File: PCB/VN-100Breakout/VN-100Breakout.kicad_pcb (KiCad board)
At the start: 4 copper layers, 2 parts, among them U1 VN-100_Breakout, U2 VN-100

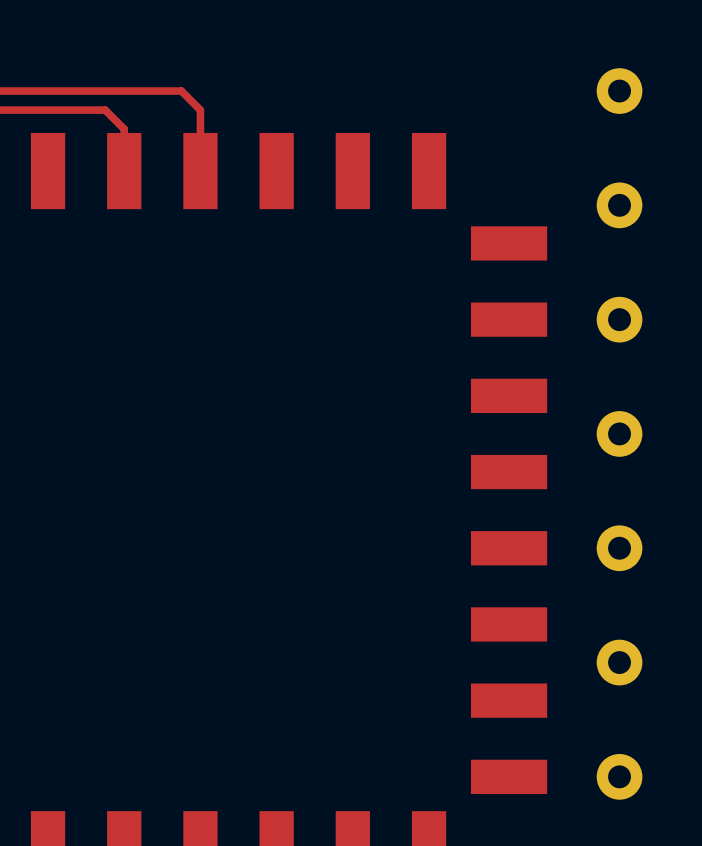
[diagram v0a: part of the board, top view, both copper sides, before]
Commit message: VN-100 edited
Connected some traces in VN-100
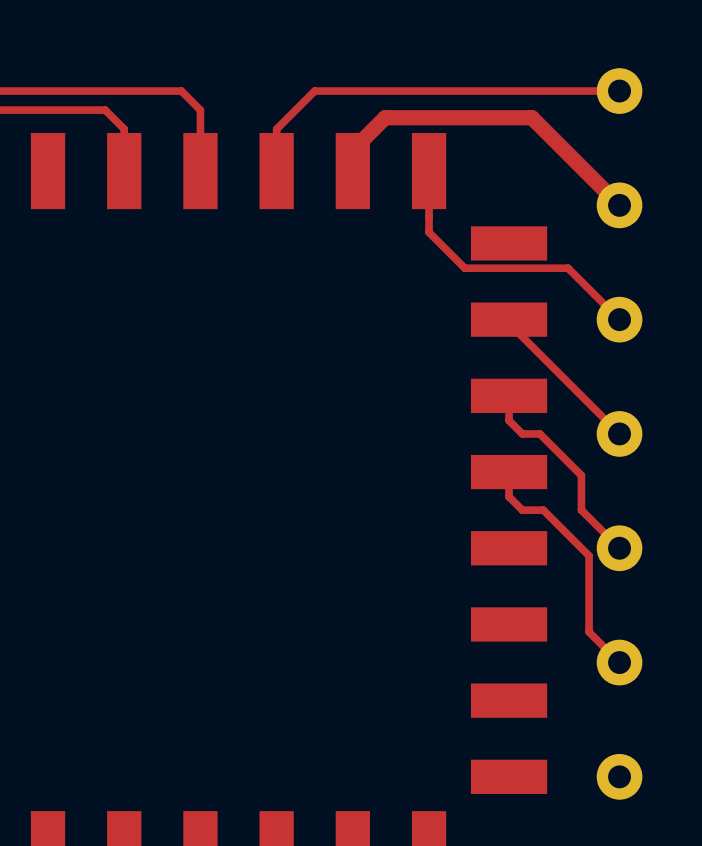
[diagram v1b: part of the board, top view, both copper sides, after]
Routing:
- net /Enable: track 0.00 -> 13.4 mm
- net /Vin: track 0.00 -> 11.2 mm
- net /SYNC_OUT: track 0.00 -> 9.60 mm
- net /RX2: track 0.00 -> 8.28 mm
- net /TX2: track 0.00 -> 6.95 mm
- net /Restore: track 0.00 -> 5.34 mm
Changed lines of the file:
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@@
-(kicad_pcb (version 20171130) (host pcbnew "(5.1.10)-1")
+(kicad_pcb (version 20171130) (host pcbnew "(5.1.5)-3")
   (general
     (thickness 1.6002)
     (drawings 1)
-    (tracks 26)
+    (tracks 52)
     (zones 0)
     (modules 2)
@@
   (segment (start 142.24 90.805) (end 139.7 93.345) (width 0.254) (layer Front) (net 8))
   (segment (start 151.13 92.837) (end 151.13 91.44) (width 0.254) (layer Front) (net 8))
+  (segment (start 167.64 90.17) (end 157.48 90.17) (width 0.254) (layer Front) (net 9))
+  (segment (start 157.48 90.17) (end 156.21 91.44) (width 0.254) (layer Front) (net 9))
+  (segment (start 156.21 91.44) (end 156.21 92.837) (width 0.254) (layer Front) (net 9))
+  (segment (start 159.8295 91.059) (end 158.75 92.1385) (width 0.508) (layer Front) (net 10))
+  (segment (start 164.719 91.059) (end 159.8295 91.059) (width 0.508) (layer Front) (net 10))
+  (segment (start 158.75 92.1385) (end 158.75 92.837) (width 0.508) (layer Front) (net 10))
+  (segment (start 167.64 93.98) (end 164.719 91.059) (width 0.508) (layer Front) (net 10))
+  (segment (start 161.29 94.361) (end 161.29 92.837) (width 0.254) (layer Front) (net 11))
+  (segment (start 161.29 94.881702) (end 161.29 94.361) (width 0.254) (layer Front) (net 11))
+  (segment (start 165.925501 96.075501) (end 162.483799 96.075501) (width 0.254) (layer Front) (net 11))
+  (segment (start 162.483799 96.075501) (end 161.29 94.881702) (width 0.254) (layer Front) (net 11))
+  (segment (start 167.64 97.79) (end 165.925501 96.075501) (width 0.254) (layer Front) (net 11))
+  (segment (start 163.957 97.917) (end 163.957 97.79) (width 0.254) (layer Front) (net 12))
+  (segment (start 167.64 101.6) (end 163.957 97.917) (width 0.254) (layer Front) (net 12))
+  (segment (start 167.64 105.41) (end 166.37 104.14) (width 0.254) (layer Front) (net 14))
+  (segment (start 166.37 102.984298) (end 164.985702 101.6) (width 0.254) (layer Front) (net 14))
+  (segment (start 166.37 104.14) (end 166.37 102.984298) (width 0.254) (layer Front) (net 14))
+  (segment (start 163.957 101.1555) (end 163.957 100.33) (width 0.254) (layer Front) (net 14))
+  (segment (start 164.4015 101.6) (end 163.957 101.1555) (width 0.254) (layer Front) (net 14))
+  (segment (start 164.985702 101.6) (end 164.4015 101.6) (width 0.254) (layer Front) (net 14))
+  (segment (start 166.623999 108.203999) (end 166.623999 105.663999) (width 0.254) (layer Front) (net 15))
+  (segment (start 167.64 109.22) (end 166.623999 108.203999) (width 0.254) (layer Front) (net 15))
+  (segment (start 166.623999 105.663999) (end 165.1 104.14) (width 0.254) (layer Front) (net 15))
+  (segment (start 163.957 103.6955) (end 163.957 102.87) (width 0.254) (layer Front) (net 15))
+  (segment (start 164.4015 104.14) (end 163.957 103.6955) (width 0.254) (layer Front) (net 15))
+  (segment (start 165.1 104.14) (end 164.4015 104.14) (width 0.254) (layer Front) (net 15))
 )

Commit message: Reworked some traces from Martin
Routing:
- net /SPI_CS: track 6.82 -> 6.01 mm
- net /Restore: track 5.34 -> 6.13 mm
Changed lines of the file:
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@@
-(kicad_pcb (version 20171130) (host pcbnew "(5.1.5)-3")
+(kicad_pcb (version 20171130) (host pcbnew "(5.1.10)-1")
   (general
     (thickness 1.6002)
     (drawings 1)
-    (tracks 52)
+    (tracks 53)
     (zones 0)
     (modules 2)
@@
   )
   (gr_line (start 151.13 93.98) (end 151.13 93.345) (layer Cmts.User) (width 0.1524))
-  (segment (start 141.605 97.79) (end 143.383 97.79) (width 0.254) (layer Front) (net 1))
-  (segment (start 139.7 99.695) (end 141.605 97.79) (width 0.254) (layer Front) (net 1))
-  (segment (start 139.7 101.6) (end 139.7 99.695) (width 0.254) (layer Front) (net 1))
+  (segment (start 143.383 97.79) (end 143.383 97.917) (width 0.254) (layer Front) (net 1))
+  (segment (start 139.7 101.6) (end 139.7 100.33) (width 0.254) (layer Front) (net 1))
+  (segment (start 139.7 100.33) (end 142.24 97.79) (width 0.254) (layer Front) (net 1))
+  (segment (start 142.24 97.79) (end 143.383 97.79) (width 0.254) (layer Front) (net 1))
   (segment (start 139.7 109.22) (end 139.7 108.585) (width 0.254) (layer Front) (net 2))
   (segment (start 140.335 107.95) (end 143.383 107.95) (width 0.254) (layer Front) (net 2))
@@
   (segment (start 140.97 102.87) (end 143.383 102.87) (width 0.254) (layer Front) (net 6))
   (segment (start 139.7 104.14) (end 140.97 102.87) (width 0.254) (layer Front) (net 6))
-  (segment (start 139.7 116.84) (end 142.24 116.84) (width 0.254) (layer Front) (net 7))
-  (segment (start 143.383 115.697) (end 143.383 113.03) (width 0.254) (layer Front) (net 7))
-  (segment (start 142.24 116.84) (end 143.383 115.697) (width 0.254) (layer Front) (net 7))
+  (segment (start 139.7 116.84) (end 139.7 115.57) (width 0.254) (layer Front) (net 7))
+  (segment (start 139.7 115.57) (end 142.24 113.03) (width 0.254) (layer Front) (net 7))
+  (segment (start 142.24 113.03) (end 143.383 113.03) (width 0.254) (layer Front) (net 7))
   (segment (start 139.7 93.345) (end 139.7 93.98) (width 0.254) (layer Front) (net 8))
   (segment (start 150.495 90.805) (end 142.24 90.805) (width 0.254) (layer Front) (net 8))
@@
   (segment (start 158.75 92.1385) (end 158.75 92.837) (width 0.508) (layer Front) (net 10))
   (segment (start 167.64 93.98) (end 164.719 91.059) (width 0.508) (layer Front) (net 10))
-  (segment (start 161.29 94.361) (end 161.29 92.837) (width 0.254) (layer Front) (net 11))
-  (segment (start 161.29 94.881702) (end 161.29 94.361) (width 0.254) (layer Front) (net 11))
-  (segment (start 165.925501 96.075501) (end 162.483799 96.075501) (width 0.254) (layer Front) (net 11))
-  (segment (start 162.483799 96.075501) (end 161.29 94.881702) (width 0.254) (layer Front) (net 11))
-  (segment (start 167.64 97.79) (end 165.925501 96.075501) (width 0.254) (layer Front) (net 11))
+  (segment (start 161.29 92.837) (end 161.29 95.25) (width 0.254) (layer Front) (net 11))
+  (segment (start 161.29 95.25) (end 162.56 96.52) (width 0.254) (layer Front) (net 11))
+  (segment (start 162.56 96.52) (end 166.37 96.52) (width 0.254) (layer Front) (net 11))
+  (segment (start 166.37 96.52) (end 167.64 97.79) (width 0.254) (layer Front) (net 11))
   (segment (start 163.957 97.917) (end 163.957 97.79) (width 0.254) (layer Front) (net 12))
-  (segment (start 167.64 101.6) (end 163.957 97.917) (width 0.254) (layer Front) (net 12))
-  (segment (start 167.64 105.41) (end 166.37 104.14) (width 0.254) (layer Front) (net 14))
-  (segment (start 166.37 102.984298) (end 164.985702 101.6) (width 0.254) (layer Front) (net 14))
-  (segment (start 166.37 104.14) (end 166.37 102.984298) (width 0.254) (layer Front) (net 14))
-  (segment (start 163.957 101.1555) (end 163.957 100.33) (width 0.254) (layer Front) (net 14))
-  (segment (start 164.4015 101.6) (end 163.957 101.1555) (width 0.254) (layer Front) (net 14))
-  (segment (start 164.985702 101.6) (end 164.4015 101.6) (width 0.254) (layer Front) (net 14))
-  (segment (start 166.623999 108.203999) (end 166.623999 105.663999) (width 0.254) (layer Front) (net 15))
-  (segment (start 167.64 109.22) (end 166.623999 108.203999) (width 0.254) (layer Front) (net 15))
-  (segment (start 166.623999 105.663999) (end 165.1 104.14) (width 0.254) (layer Front) (net 15))
-  (segment (start 163.957 103.6955) (end 163.957 102.87) (width 0.254) (layer Front) (net 15))
-  (segment (start 164.4015 104.14) (end 163.957 103.6955) (width 0.254) (layer Front) (net 15))
-  (segment (start 165.1 104.14) (end 164.4015 104.14) (width 0.254) (layer Front) (net 15))
+  (segment (start 167.64 101.6) (end 166.37 100.33) (width 0.254) (layer Front) (net 12))
+  (segment (start 166.37 100.33) (end 166.37 99.06) (width 0.254) (layer Front) (net 12))
+  (segment (start 165.1 97.79) (end 163.957 97.79) (width 0.254) (layer Front) (net 12))
+  (segment (start 166.37 99.06) (end 165.1 97.79) (width 0.254) (layer Front) (net 12))
+  (segment (start 167.64 105.41) (end 167.64 104.14) (width 0.254) (layer Front) (net 14))
+  (segment (start 167.64 104.14) (end 166.37 102.87) (width 0.254) (layer Front) (net 14))
+  (segment (start 166.37 102.87) (end 166.37 101.6) (width 0.254) (layer Front) (net 14))
+  (segment (start 166.37 101.6) (end 165.1 100.33) (width 0.254) (layer Front) (net 14))
+  (segment (start 165.1 100.33) (end 163.957 100.33) (width 0.254) (layer Front) (net 14))
+  (segment (start 167.64 109.22) (end 167.64 107.95) (width 0.254) (layer Front) (net 15))
+  (segment (start 167.64 107.95) (end 166.37 106.68) (width 0.254) (layer Front) (net 15))
+  (segment (start 166.37 106.68) (end 166.37 104.14) (width 0.254) (layer Front) (net 15))
+  (segment (start 166.37 104.14) (end 165.1 102.87) (width 0.254) (layer Front) (net 15))
+  (segment (start 165.1 102.87) (end 163.957 102.87) (width 0.254) (layer Front) (net 15))
 )

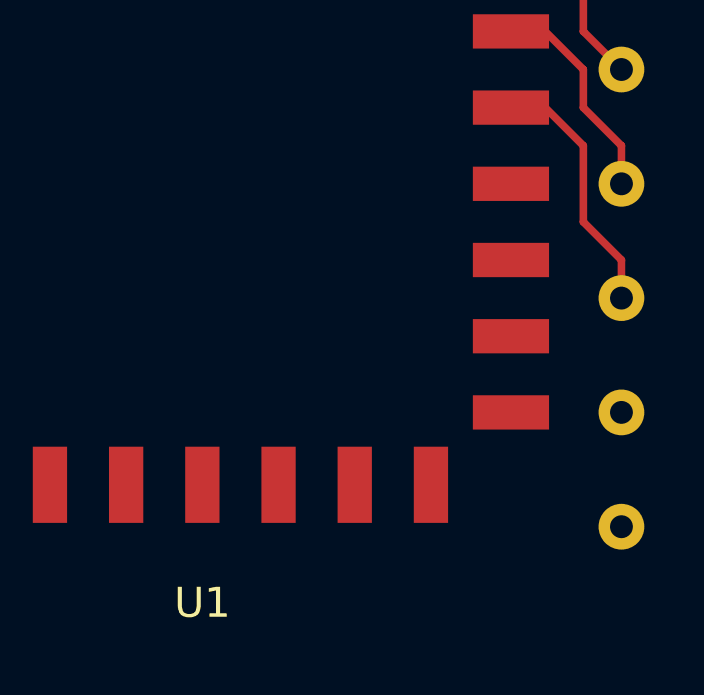
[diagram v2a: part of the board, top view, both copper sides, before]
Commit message: Connected ground to pads
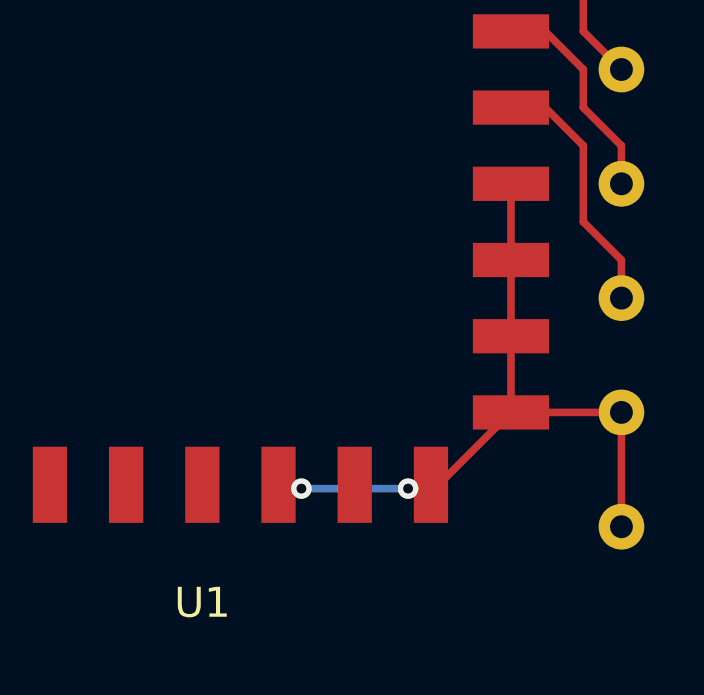
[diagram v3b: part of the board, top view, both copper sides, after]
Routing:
- net /GND: track 0.00 -> 24.0 mm, vias 0 -> 2
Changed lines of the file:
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@@
     (thickness 1.6002)
     (drawings 1)
-    (tracks 53)
+    (tracks 65)
     (zones 0)
     (modules 2)
@@
   )
   (gr_line (start 151.13 93.98) (end 151.13 93.345) (layer Cmts.User) (width 0.1524))
+  (via (at 160.528 115.57) (size 0.6858) (drill 0.3302) (layers Front Back) (net 13))
+  (via (at 156.972 115.57) (size 0.6858) (drill 0.3302) (layers Front Back) (net 13))
   (segment (start 143.383 97.79) (end 143.383 97.917) (width 0.254) (layer Front) (net 1))
   (segment (start 139.7 101.6) (end 139.7 100.33) (width 0.254) (layer Front) (net 1))
@@
   (segment (start 165.1 97.79) (end 163.957 97.79) (width 0.254) (layer Front) (net 12))
   (segment (start 166.37 99.06) (end 165.1 97.79) (width 0.254) (layer Front) (net 12))
+  (segment (start 163.957 105.41) (end 163.957 113.03) (width 0.254) (layer Front) (net 13))
+  (segment (start 163.957 113.03) (end 167.64 113.03) (width 0.254) (layer Front) (net 13))
+  (segment (start 167.64 116.84) (end 167.64 113.03) (width 0.254) (layer Front) (net 13))
+  (segment (start 161.544 115.443) (end 163.957 113.03) (width 0.254) (layer Front) (net 13))
+  (segment (start 161.29 115.443) (end 161.544 115.443) (width 0.254) (layer Front) (net 13))
+  (segment (start 156.845 115.443) (end 156.972 115.57) (width 0.254) (layer Front) (net 13))
+  (segment (start 156.21 115.443) (end 156.845 115.443) (width 0.254) (layer Front) (net 13))
+  (segment (start 156.972 115.57) (end 160.528 115.57) (width 0.254) (layer Back) (net 13))
+  (segment (start 160.655 115.443) (end 160.528 115.57) (width 0.254) (layer Front) (net 13))
+  (segment (start 161.29 115.443) (end 160.655 115.443) (width 0.254) (layer Front) (net 13))
   (segment (start 167.64 105.41) (end 167.64 104.14) (width 0.254) (layer Front) (net 14))
   (segment (start 167.64 104.14) (end 166.37 102.87) (width 0.254) (layer Front) (net 14))

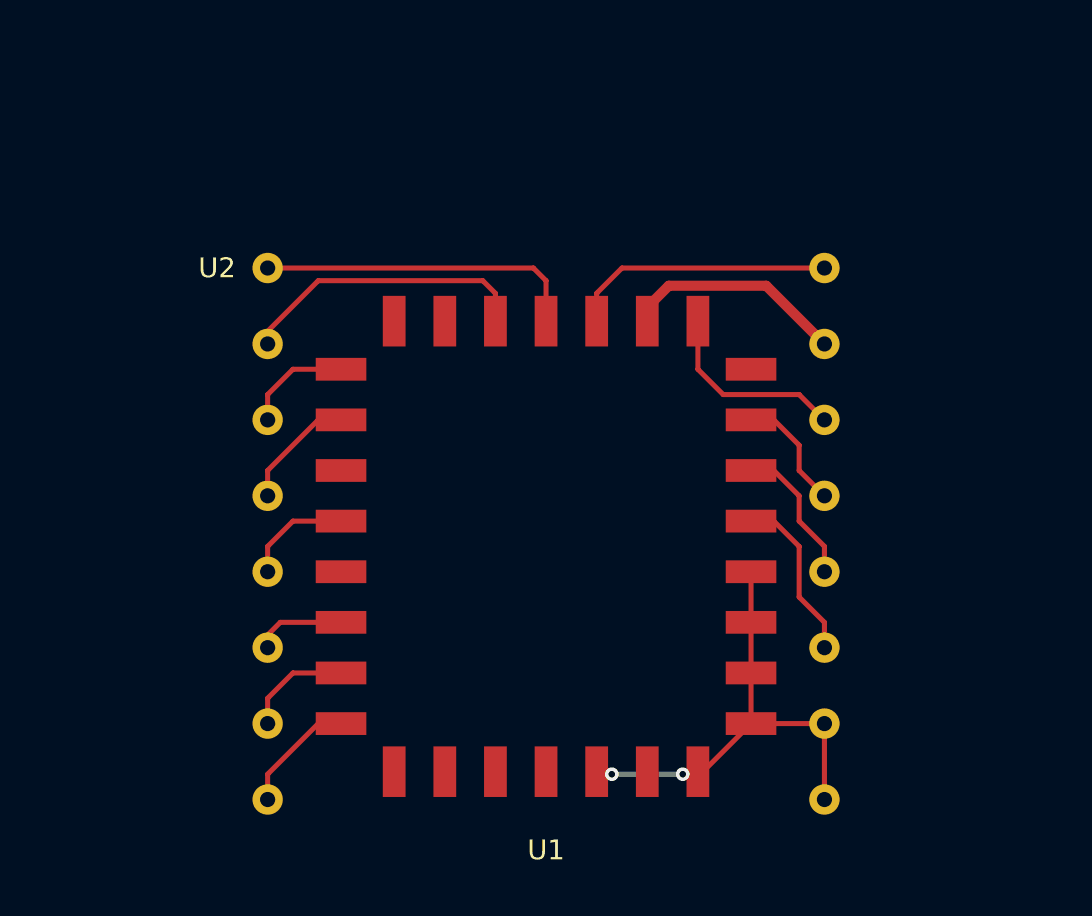
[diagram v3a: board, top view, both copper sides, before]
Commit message: Finished VN-100 Breakout Board. Removed USB from DevBoard Schematic
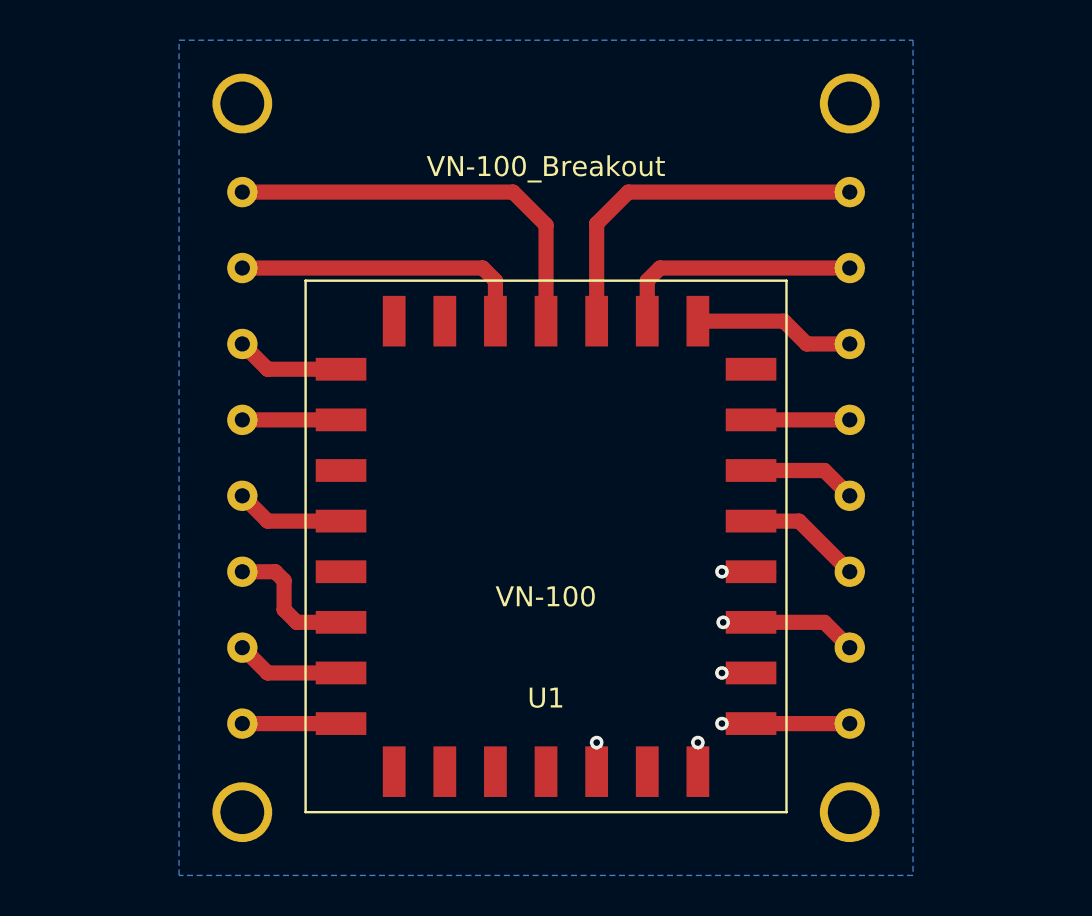
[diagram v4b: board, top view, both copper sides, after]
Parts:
- moved U1 3.81 mm to (153.7, 99.1)
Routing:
- net /Enable: track 13.4 -> 18.2 mm
- net /TX1: track 16.3 -> 20.7 mm
- net /GND: track 24.0 -> 20.6 mm, vias 2 -> 6
- net /NRST: track 4.58 -> 7.11 mm
- net /Vin: track 11.2 -> 13.2 mm
- net /RX2: track 8.55 -> 6.89 mm
- net /SYNC_OUT: track 9.82 -> 8.27 mm
- net /SPI_CS: track 6.01 -> 4.95 mm
- net /SPI_MOSI: track 6.13 -> 5.08 mm
- net /TX2: track 7.28 -> 6.62 mm
- added copper zone on B.Cu, net /GND
